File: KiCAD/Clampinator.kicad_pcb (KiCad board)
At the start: 4 copper layers, 200 x 130 mm, 194 parts, among them J1 Power, J10 Conn_01x04, J11 Conn_01x04, J12 FDCAN_1, J13 FDCAN_2, J14 10k NTC, J15 10k NTC, J16 EN_NTC_B, J17 EN_NTC_A, J18 FAN, J19 FAN, J20 VP0265840000G, J23 VP0265840000G, J24 VP0265840000G, J25 +5V INJ, J5 Debug Header, J6 Conn_01x04, J7 Conn_01x04, J8 Conn_01x04, J9 Conn_01x04, Q1 TK100E10N1,S1X, Q10 AO3400A, Q2 TK100E10N1,S1X, Q3 TK100E10N1,S1X, Q4 TK100E10N1,S1X, Q5 TK100E10N1,S1X, Q6 AO3400A, Q7 AO3400A, Q8 AO3400A, Q9 MMBT3904-C20526, SW1 PTS810SJM250SMTRLFS, SW2 PTS810SJM250SMTRLFS, SW3 PTS810SJM250SMTRLFS, SW4 PTS810SJM250SMTRLFS, SW5 SMQS-02R-TP, SW6 EG1847-ND, SW7 GPI-154-3013, U1 STM32H573RIT6, U10 LM74810QDRRRQ1, U12 TPS7A2033DQNR, U13 VOS618A-3T, U14 LM5163DDAR, U2 TL432BQDBZR, U3 EG2131, U4 UCC33420RAQR_C46461551, U5 USBLC6-2SC6, U6 LM5012DDAR, U7 MCP2562FD-E/P, U8 MCP2562FD-E/P, U9 EL357N, X1 SC-32S32.768kHz20PPM7pF, Y2 ECS-80-18-23B-JTM-TR

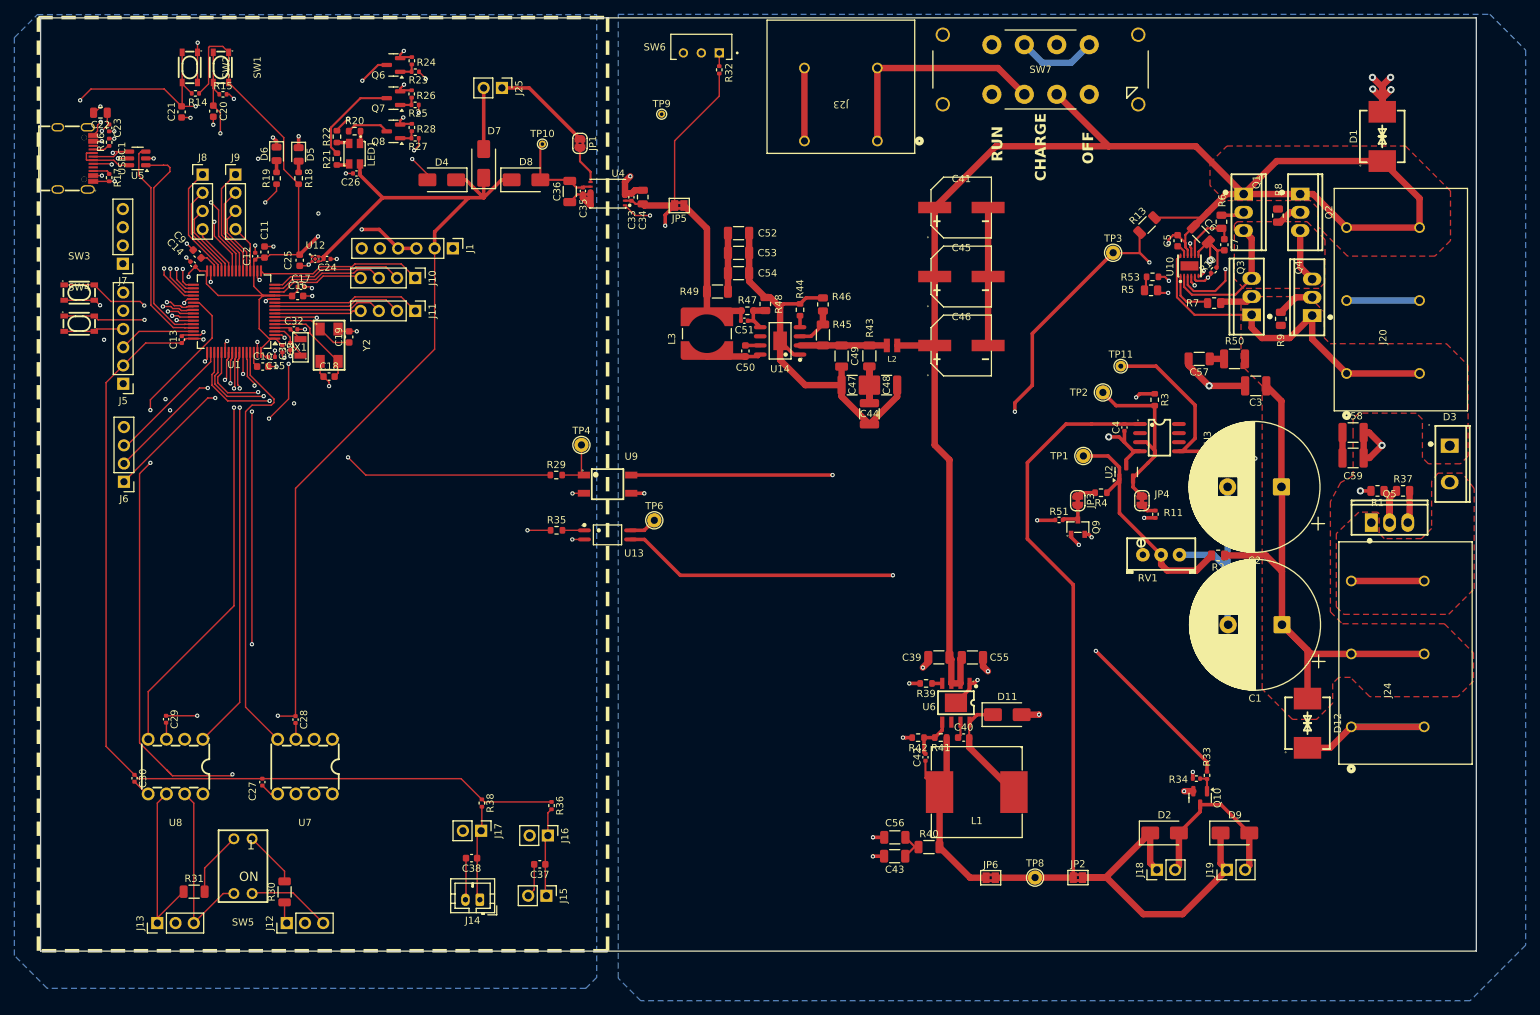
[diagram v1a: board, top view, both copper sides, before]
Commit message: Fix all DRC errors
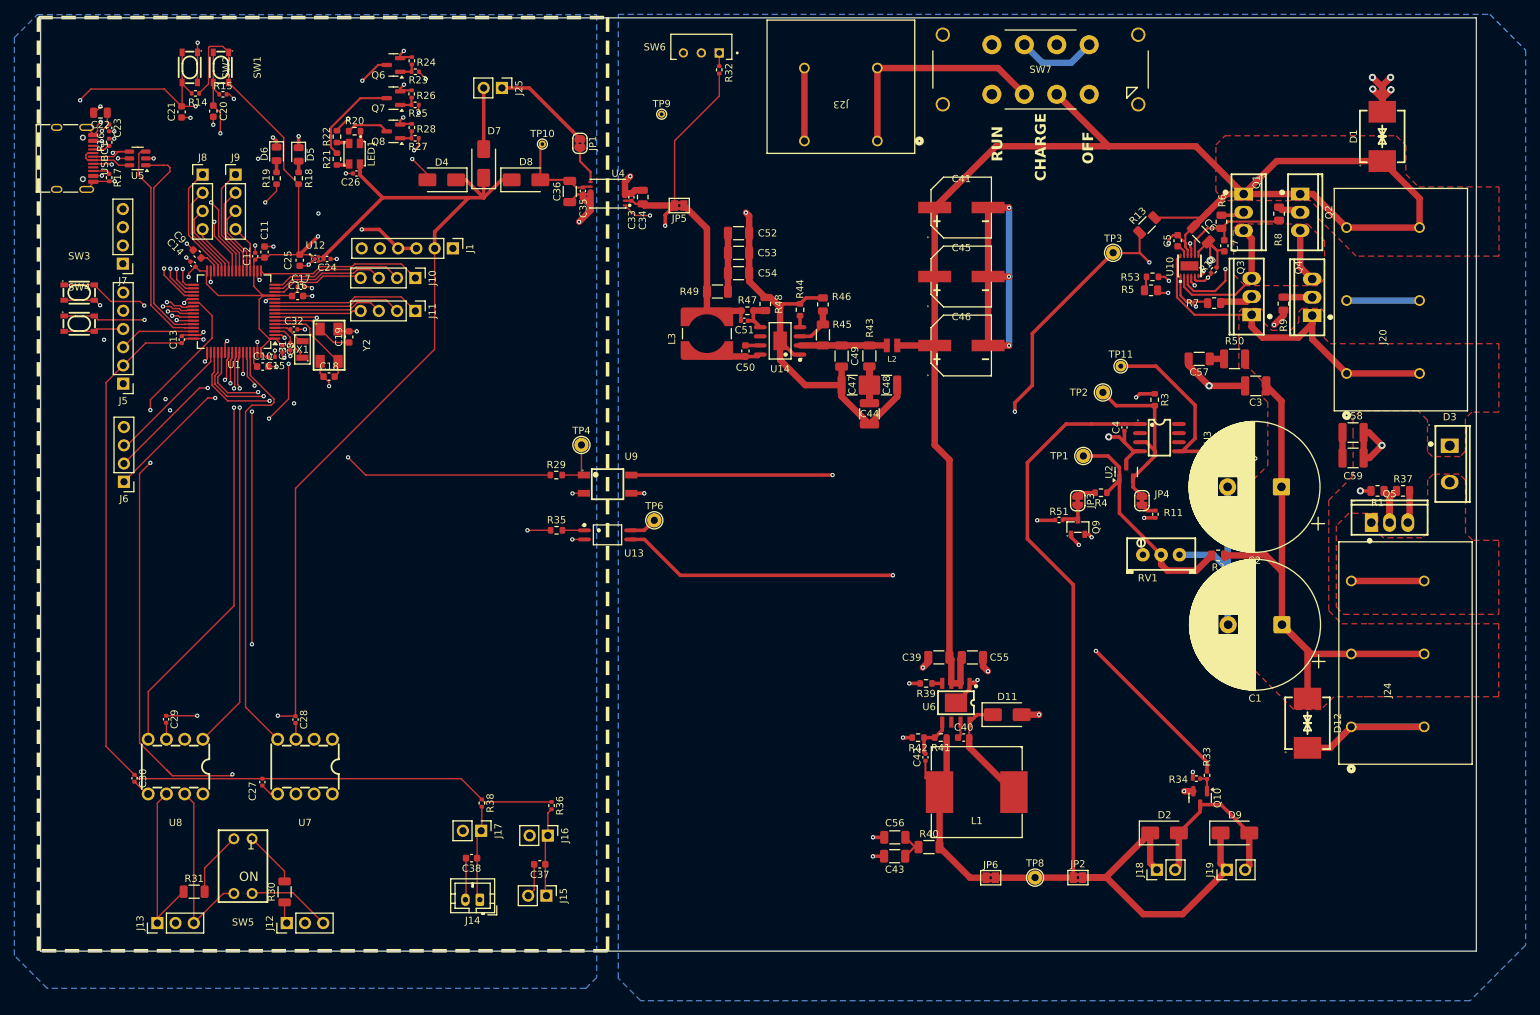
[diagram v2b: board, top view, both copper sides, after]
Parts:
- USBC1: footprint easyeda2kicad:USB-C_SMD-TYPE-C-31-M-12_1 -> Connector_USB:USB_C_Receptacle_HRO_TYPE-C-31-M-12
- moved R9 2.15 mm to (220.9, 64.3)
- moved USBC1 1.57 mm to (51.1, 44.1)
- moved X1 0.41 mm to (84.3, 70.7)
- moved R8 0.30 mm to (220.3, 51.8), turned to -90 degrees
- moved C7 0.15 mm to (212.7, 56.3)
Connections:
- Y2 pad 4: (no net) -> GND
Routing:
- net DC_GND: track 242.3 -> 273.4 mm, vias 21 -> 25
- net DGATE: track 6.94 -> 23.5 mm, vias 0 -> 2
- net HGATE: track 8.20 -> 16.8 mm
- net GND: track 109.9 -> 116.3 mm, vias 39 -> 40
- net +3V3: track 251.4 -> 253.2 mm
- net Net-(Q4-G): track 5.23 -> 4.02 mm
- net NRST: track 101.1 -> 101.8 mm
- net BRAKE_A: track 371.3 -> 371.8 mm

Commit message: Moved most of silkscreens into readable areas, moved some footprints for hand-soldering
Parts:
- moved C52 2.94 mm to (145.0, 51.6)
- moved C53 2.37 mm to (145.0, 54.9)
- moved R32 2.26 mm to (142.3, 34.0)
- moved C54 1.77 mm to (145.0, 58.3)
- moved R48 1.44 mm to (150.0, 65.1), turned to 0 degrees
- moved R49 1.09 mm to (142.1, 61.6)
- moved C36 0.85 mm to (120.7, 48.6)
- moved R44 0.83 mm to (153.6, 64.4)
- moved C34 0.75 mm to (132.4, 49.7)
- moved L3 0.73 mm to (139.9, 68.5)
- moved C51 0.66 mm to (145.8, 67.4)
- moved C50 0.53 mm to (145.4, 70.9)
- moved R9 0.48 mm to (220.4, 64.3)
- moved C33 0.48 mm to (130.6, 49.5)
- moved C35 0.42 mm to (122.9, 48.5)
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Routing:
- net DC_GND: track 273.4 -> 275.8 mm
- net Net-(SW6-A): track 1.85 -> 4.11 mm
- net +5VR: track 164.0 -> 161.9 mm
- net Net-(JP5-A): track 22.2 -> 23.6 mm
- net GND: track 116.3 -> 115.1 mm
- net Net-(U14-FB): track 6.47 -> 7.58 mm
- net CAN1_STBY: track 97.9 -> 97.0 mm
- net Net-(U14-RON): track 1.60 -> 2.43 mm
- net Net-(U14-SW): track 7.55 -> 8.28 mm
- net Net-(U14-BST): track 2.07 -> 2.60 mm
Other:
- board text added: "CLAMP"
- board text added: "ON"

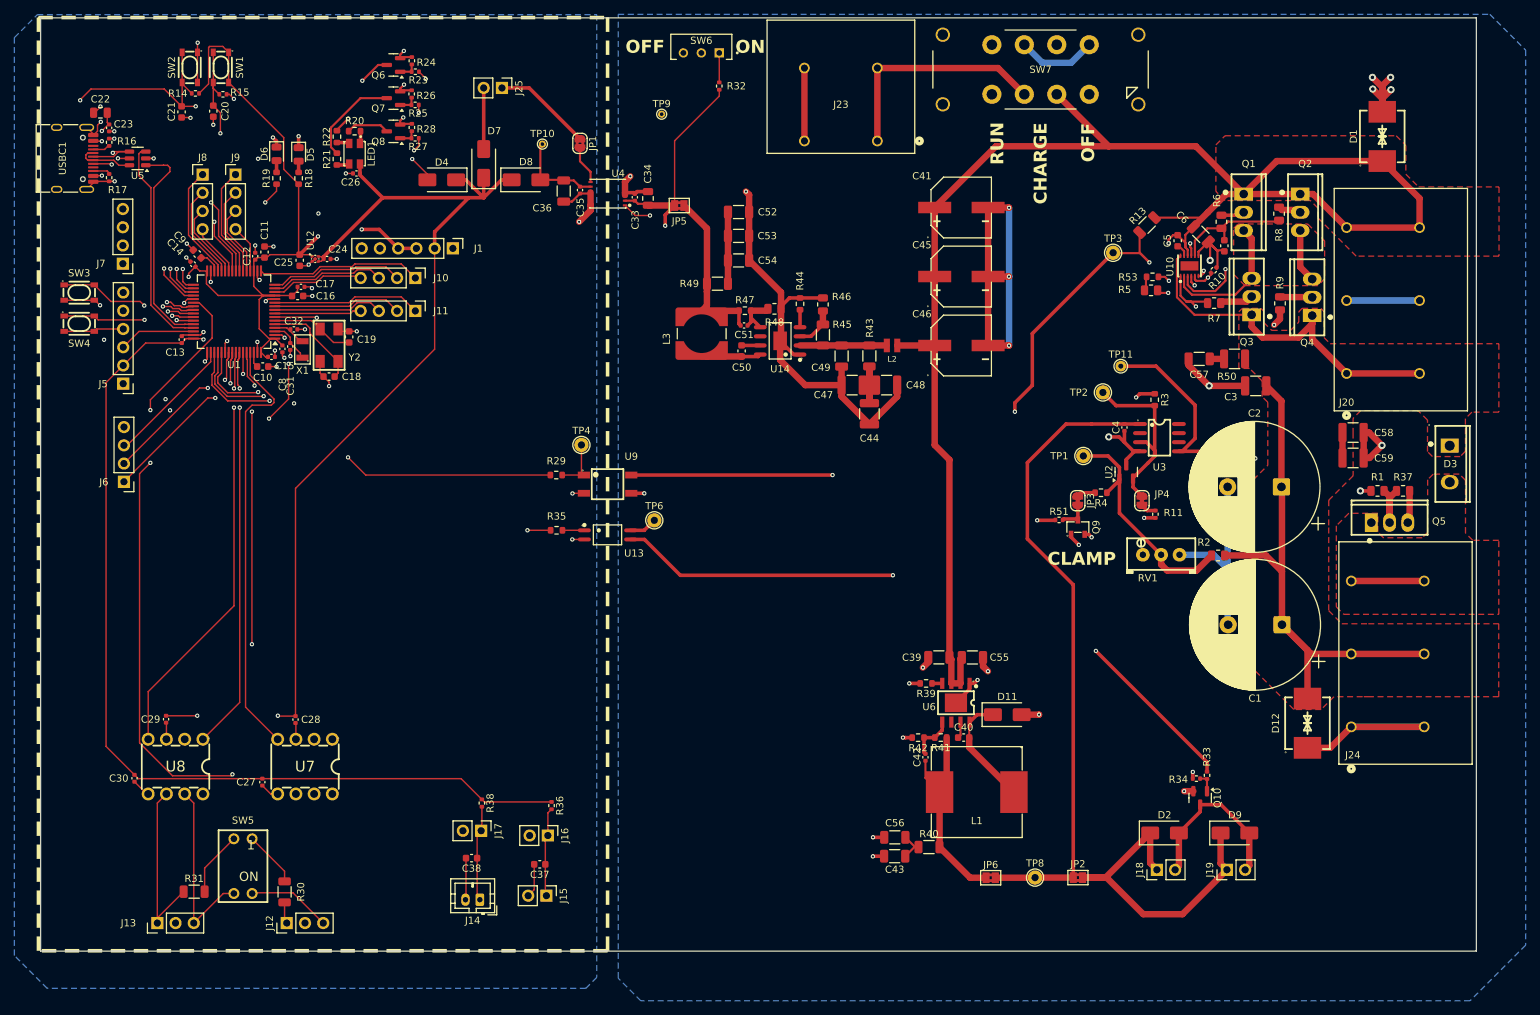
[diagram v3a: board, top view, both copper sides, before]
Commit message: Labels, silkscreens, shifted footprints
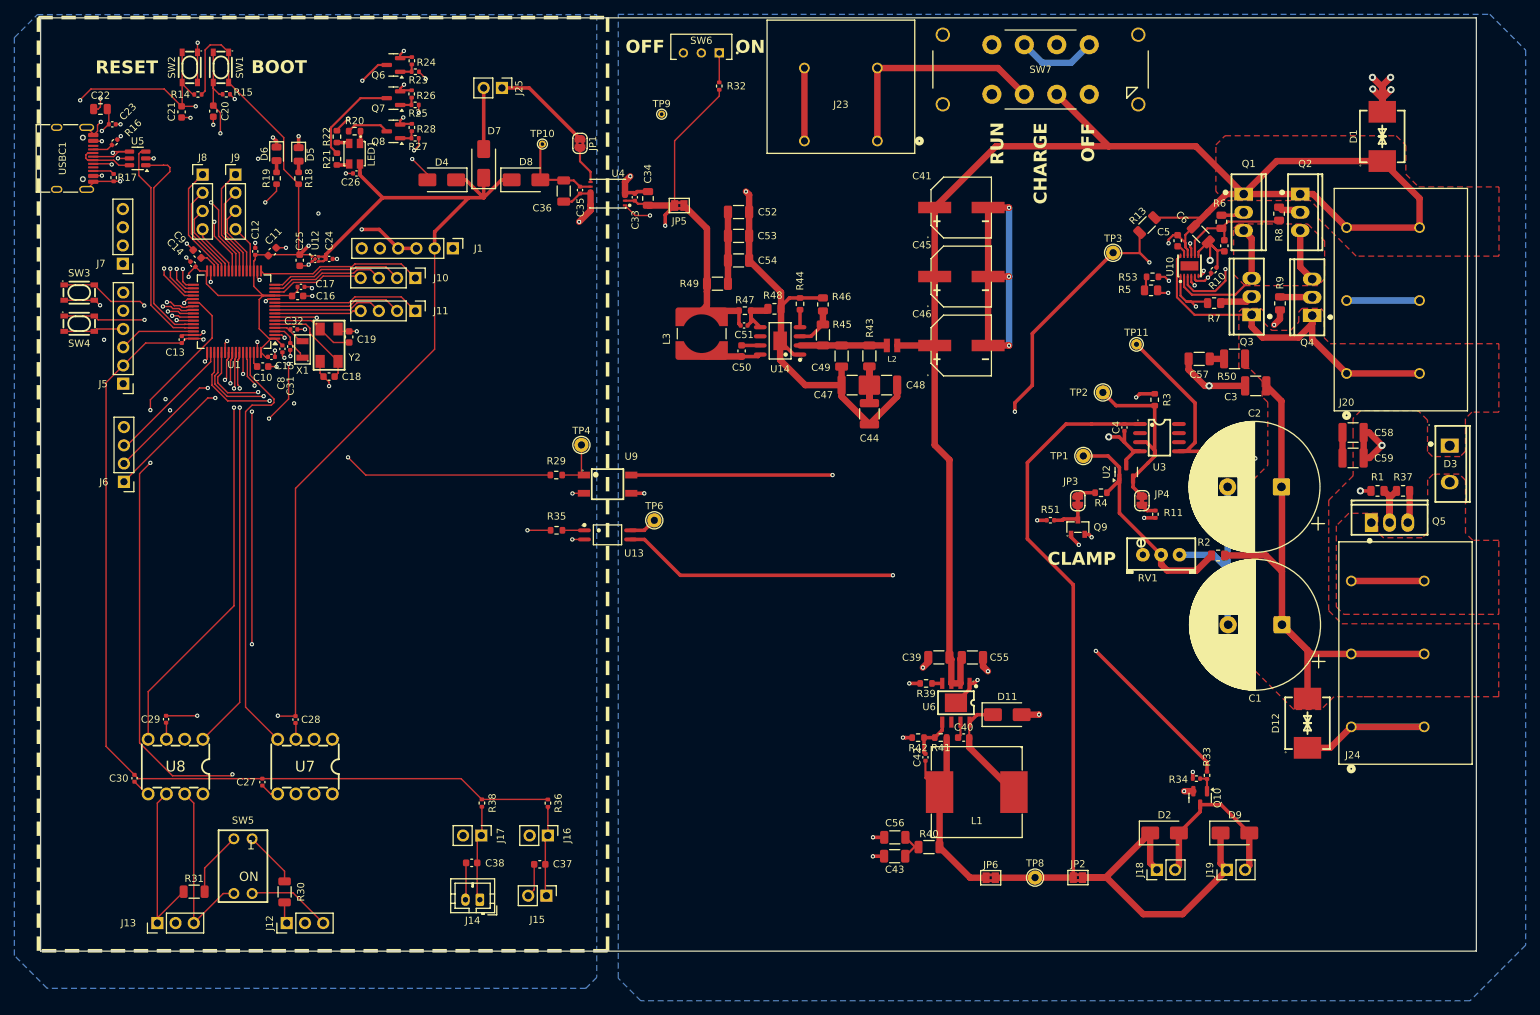
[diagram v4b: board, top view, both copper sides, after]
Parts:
- moved TP11 3.75 mm to (200.5, 70.0)
- moved R51 1.20 mm to (188.5, 94.5)
- moved C11 1.08 mm to (80.1, 57.1), turned to 45 degrees
- moved R16 0.76 mm to (58.1, 41.9), turned to 45 degrees
- moved C12 0.67 mm to (77.7, 57.1)
- moved C23 0.66 mm to (57.8, 39.4), turned to 0 degrees
- moved C38 0.66 mm to (107.9, 142.2)
- moved J17 0.66 mm to (109.2, 138.4)
- moved R17 0.63 mm to (58.0, 46.8)
- moved R36 0.61 mm to (118.5, 133.9)
- moved C22 0.51 mm to (56.1, 37.2)
- moved R15 0.47 mm to (73.7, 35.2)
- moved R14 0.38 mm to (69.7, 35.2)
- moved C24 0.29 mm to (88.0, 58.1)
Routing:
- net +5VR: track 161.9 -> 160.7 mm
- net Net-(JP3-B): track 4.26 -> 5.48 mm
- net NTC_A_IN: track 118.8 -> 119.5 mm
- net Net-(USBC1-CC2): track 2.49 -> 3.02 mm
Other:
- board text added: "BOOT"
- board text added: "RESET"
